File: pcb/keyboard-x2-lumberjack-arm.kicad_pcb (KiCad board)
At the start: 2 copper layers, 285 x 94.2 mm, 141 parts, among them J1 16-pin USB-C Connector SMD, U1 STM32F103 Bluepill, or MiniF4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, U2 SN74LVC1T45DBV

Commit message: feat: 1U hotswap sw5-1 - sw5-12
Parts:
- SW_5_1, SW_5_10, SW_5_11, SW_5_12, SW_5_2, SW_5_3, SW_5_4, SW_5_5, SW_5_6, SW_5_7, SW_5_8, SW_5_9: footprint ProjectLocal:SW_MX_PG1350_NoLed -> ProjectLocal:MXOnly-1U-Hotswap-180
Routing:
- net /COL3: track 191.4 -> 180.8 mm, vias 14 -> 15
- net /COL1: track 239.4 -> 229.3 mm, vias 14 -> 15
- net /COL10: track 221.4 -> 211.2 mm, vias 14 -> 15
- net /COL11: track 237.8 -> 228.1 mm, vias 14 -> 15
- net /COL4: track 171.1 -> 161.5 mm, vias 14 -> 15
- net /COL8: track 182.6 -> 173.1 mm, vias 14 -> 15
- net /COL5: track 152.8 -> 143.4 mm, vias 14 -> 15
- net /COL9: track 203.2 -> 193.9 mm, vias 14 -> 15
- net /COL2: track 212.8 -> 204.0 mm, vias 14 -> 15
- net /COL7: track 141.5 -> 133.6 mm, vias 14 -> 15
- net /COL12: track 232.8 -> 226.6 mm, vias 4 -> 5
- net /COL6: track 129.9 -> 123.8 mm, vias 14 -> 15
- net Net-(D_5_6-Pad2): track 55.0 -> 51.4 mm, vias 0 -> 1
- net Net-(D_5_9-Pad2): track 75.2 -> 73.3 mm, vias 0 -> 1
- net Net-(D_5_11-Pad2): track 107.3 -> 105.4 mm, vias 0 -> 1
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
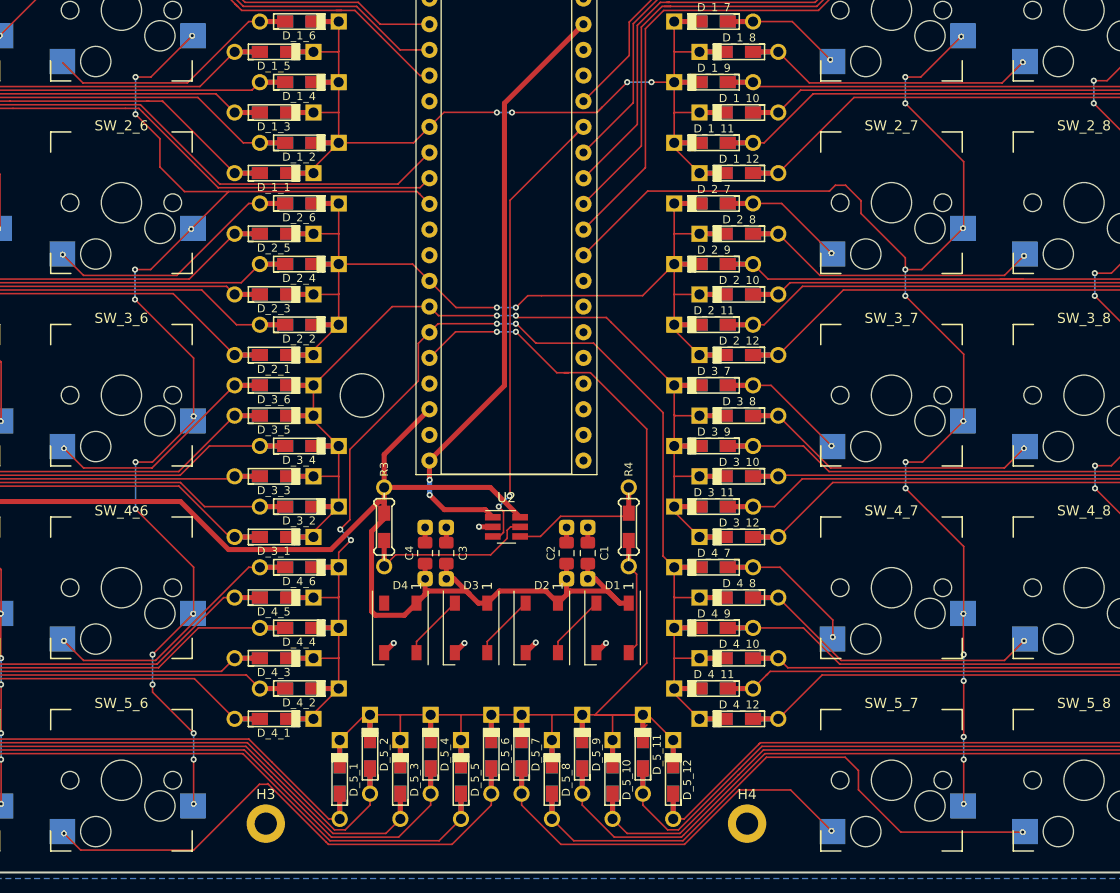
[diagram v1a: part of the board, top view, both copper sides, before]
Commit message: fix: unconnected pad
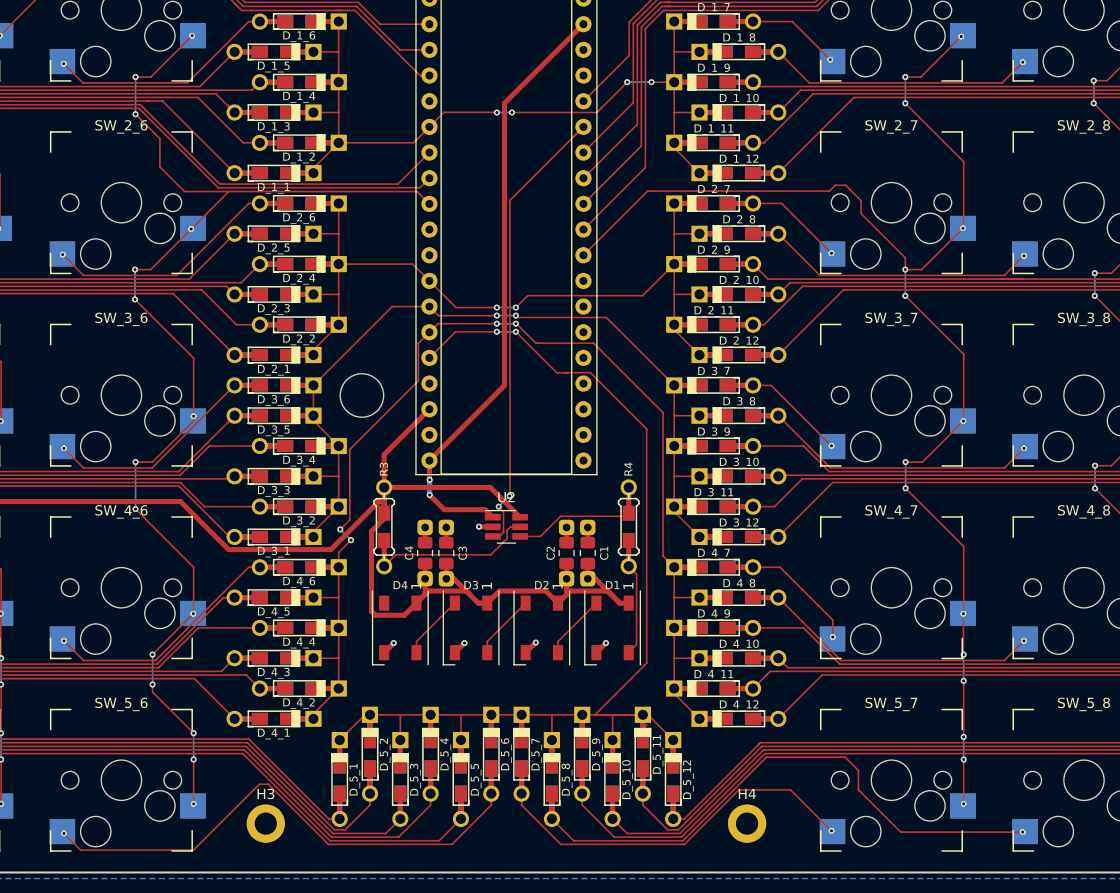
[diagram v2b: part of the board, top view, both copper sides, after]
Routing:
- net Net-(D_5_8-Pad2): track 57.0 -> 55.6 mm
- net Net-(D_5_7-Pad2): track 39.0 -> 37.6 mm
- net Net-(D_1_6-Pad2): track 22.9 -> 23.1 mm, vias 0 -> 1
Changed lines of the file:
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@@
   (segment (start 150.589001 66.071001) (end 160.930597 66.071001) (width 0.16) (layer "F.Cu") (net 24))
   (segment (start 167.001598 60) (end 168.1 60) (width 0.16) (layer "F.Cu") (net 24))
-  (segment (start 148.582 64.064) (end 150.589001 66.071001) (width 0.16) (layer "F.Cu") (net 24))
+  (segment (start 148.582 64.064) (end 148.685 64.167) (width 0.16) (layer "F.Cu") (net 24))
+  (segment (start 148.685 64.167) (end 150.589001 66.071001) (width 0.16) (layer "F.Cu") (net 24))
+  (via (at 148.685 64.167) (size 0.6) (drill 0.3) (layers "F.Cu" "B.Cu") (net 24))
+  (segment (start 148.558 64.04) (end 148.685 64.167) (width 0.16) (layer "B.Cu") (net 24))
+  (segment (start 148.558 63.955) (end 148.558 64.04) (width 0.16) (layer "B.Cu") (net 24))
   (segment (start 190.939012 112.76999) (end 181.53001 112.76999) (width 0.16) (layer "F.Cu") (net 25))
   (segment (start 193.85 110) (end 192.91 110) (width 0.16) (layer "F.Cu") (net 25))
@@
   (segment (start 194 137.53137) (end 197.888669 141.420039) (width 0.16) (layer "F.Cu") (net 78))
   (segment (start 215.499995 136.036595) (end 220.618595 136.036595) (width 0.16) (layer "F.Cu") (net 78))
-  (segment (start 226.68 140.155) (end 228.06 140.155) (width 0.16) (layer "F.Cu") (net 78))
   (via (at 224.663 140.081) (size 0.6) (drill 0.3) (layers "F.Cu" "B.Cu") (net 78))
   (segment (start 224.737 140.155) (end 224.663 140.081) (width 0.16) (layer "B.Cu") (net 78))
@@
   (segment (start 226.019099 132.801099) (end 218.226361 132.801099) (width 0.16) (layer "F.Cu") (net 79))
   (segment (start 231.521 140.208) (end 227.33 136.017) (width 0.16) (layer "F.Cu") (net 79))
-  (segment (start 245.73 140.155) (end 247.11 140.155) (width 0.16) (layer "F.Cu") (net 79))
   (segment (start 227.33 134.112) (end 226.019099 132.801099) (width 0.16) (layer "F.Cu") (net 79))
   (segment (start 243.586 140.208) (end 231.521 140.208) (width 0.16) (layer "F.Cu") (net 79))

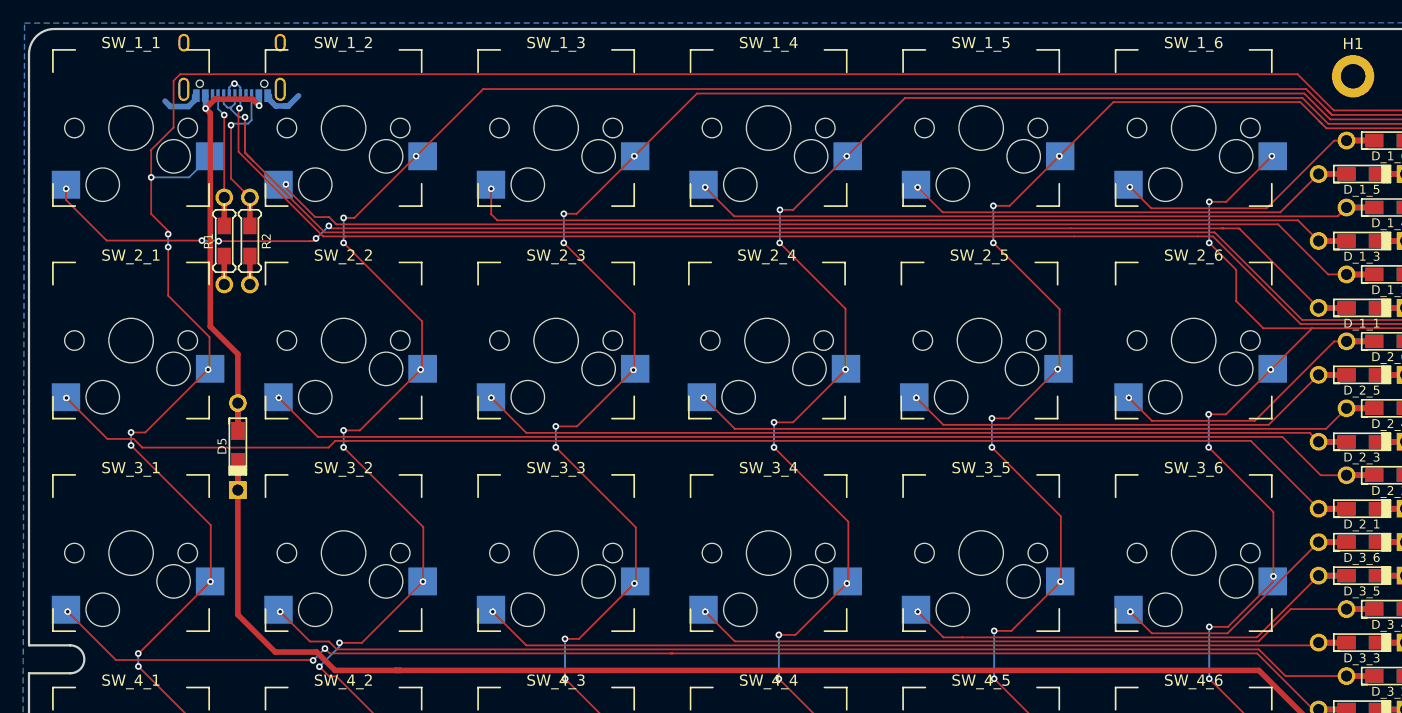
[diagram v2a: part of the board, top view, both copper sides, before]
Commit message: fix: change switch symbol value to mx hotswap
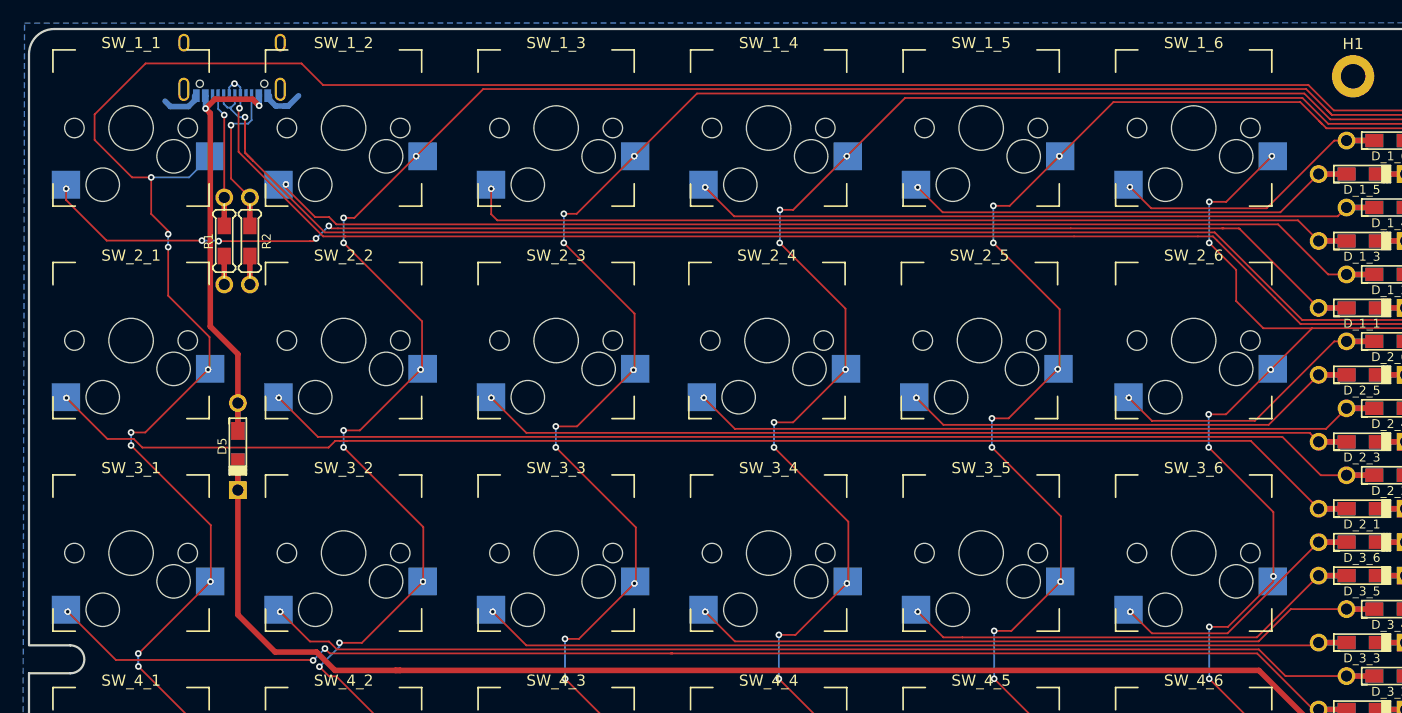
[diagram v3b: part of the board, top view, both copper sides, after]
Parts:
- SW_1_1, SW_1_10, SW_1_11, SW_1_12, SW_1_2, SW_1_3, SW_1_4, SW_1_5, SW_1_6, SW_1_7, SW_1_8, SW_1_9, SW_2_1, SW_2_10, SW_2_11, SW_2_12, SW_2_2, SW_2_3, SW_2_4, SW_2_5, SW_2_6, SW_2_7, SW_2_8, SW_2_9, SW_3_1, SW_3_10, SW_3_11, SW_3_12, SW_3_2, SW_3_3, SW_3_4, SW_3_5, SW_3_6, SW_3_7, SW_3_8, SW_3_9, SW_4_1, SW_4_10, SW_4_11, SW_4_12, SW_4_2, SW_4_3, SW_4_4, SW_4_5, SW_4_6, SW_4_7, SW_4_8, SW_4_9, SW_5_1, SW_5_10, SW_5_11, SW_5_12, SW_5_2, SW_5_3, SW_5_4, SW_5_5, SW_5_6, SW_5_7, SW_5_8, SW_5_9: value MX-compatible or Kailh Choc v1 -> MX Hotswap
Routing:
- net /COL1: track 229.3 -> 237.7 mm

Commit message: chore: tidy up routing
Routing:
- net /COL2: track 204.0 -> 181.2 mm
- net /COL10: track 211.2 -> 190.1 mm
- net /COL9: track 193.9 -> 173.3 mm
- net /COL11: track 228.1 -> 207.5 mm
- net /COL3: track 180.8 -> 162.1 mm
- net /COL5: track 143.4 -> 125.4 mm
- net /COL4: track 161.5 -> 143.6 mm
- net /COL8: track 173.1 -> 155.3 mm
- net /COL7: track 133.6 -> 120.6 mm
- net /COL1: track 237.7 -> 226.6 mm
- net /COL6: track 123.8 -> 117.1 mm
- net Net-(D_5_7-Pad2): track 37.6 -> 41.9 mm
- net Net-(D_1_12-Pad2): track 105.4 -> 107.5 mm
- net Net-(D_4_5-Pad2): track 40.0 -> 41.4 mm
- net Net-(D_1_3-Pad2): track 78.1 -> 76.7 mm
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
